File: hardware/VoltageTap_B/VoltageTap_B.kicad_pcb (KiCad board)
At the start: 2 copper layers, 154 parts, among them J1 Conn_01x09_Socket, J102 Conn_01x18_Pin, J15 Conn_02x04_Odd_Even, J16 USB_B_Micro, J2 Conn_02x05_Odd_Even, J3 Conn_01x04_Socket, Q6 2N7002, U10 MCP2542FDxMF, U12 FT230XS, U2 MCU-MSM0G3507SPM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

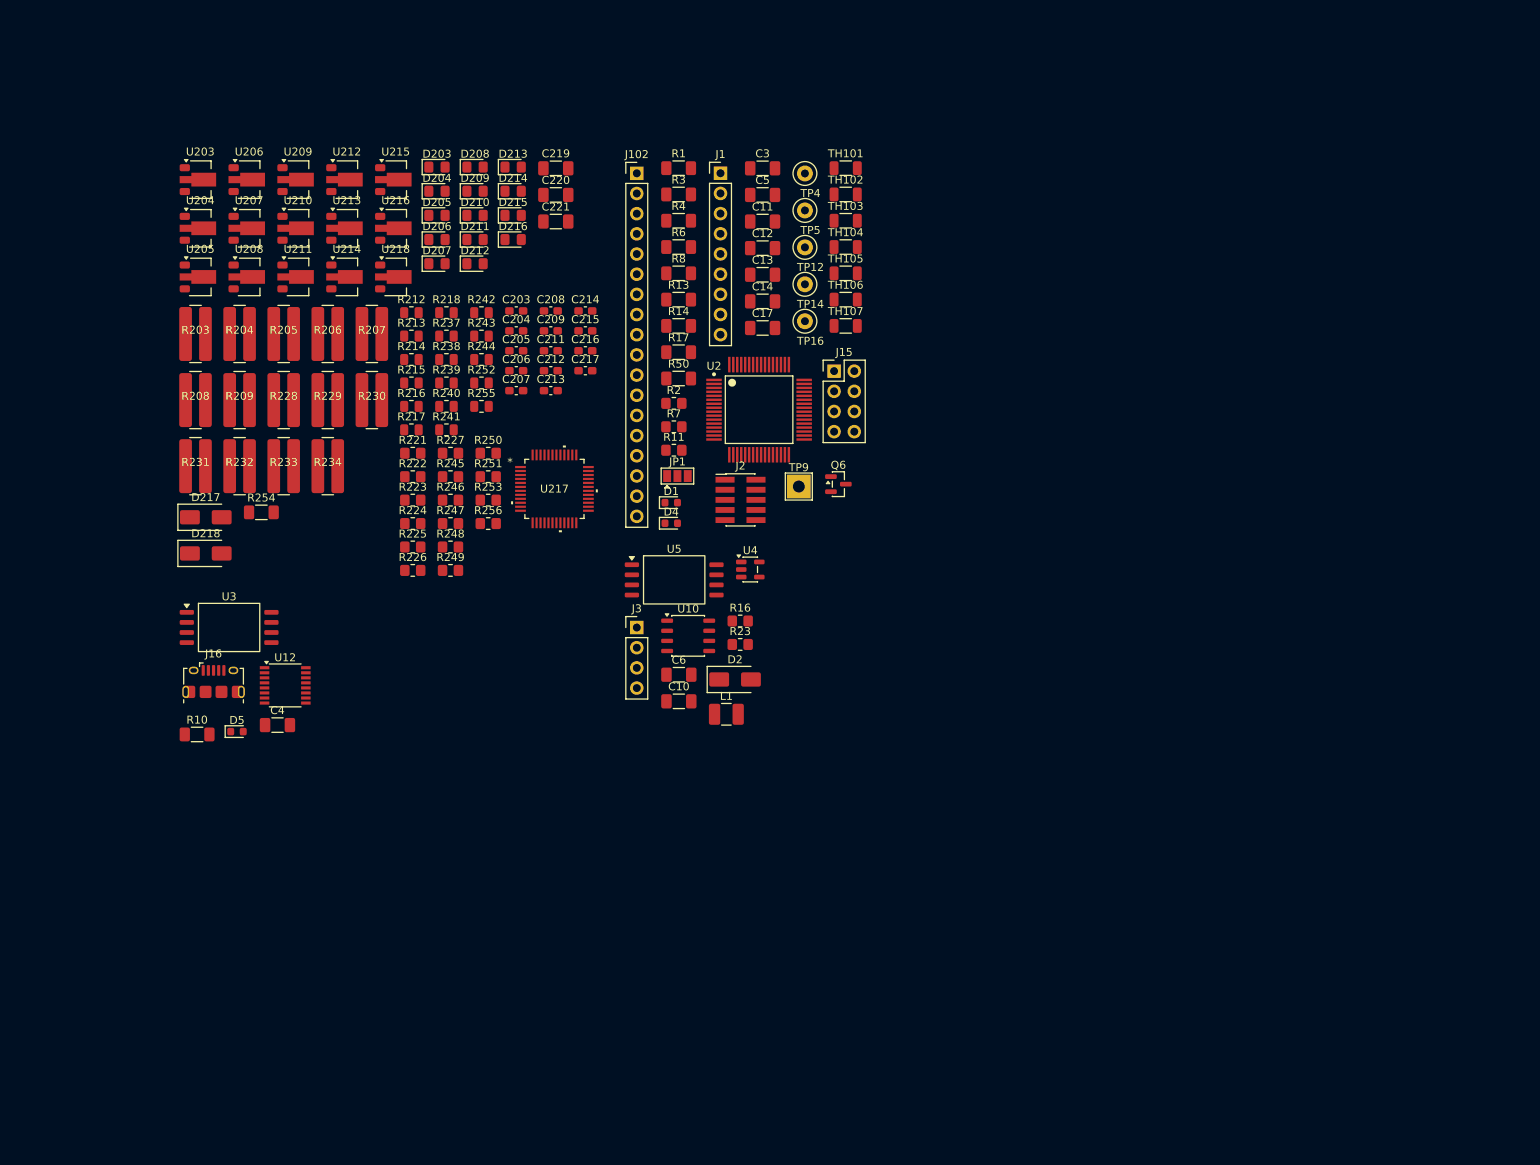
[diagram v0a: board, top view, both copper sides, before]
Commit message: voltage tap LV done. moving on.
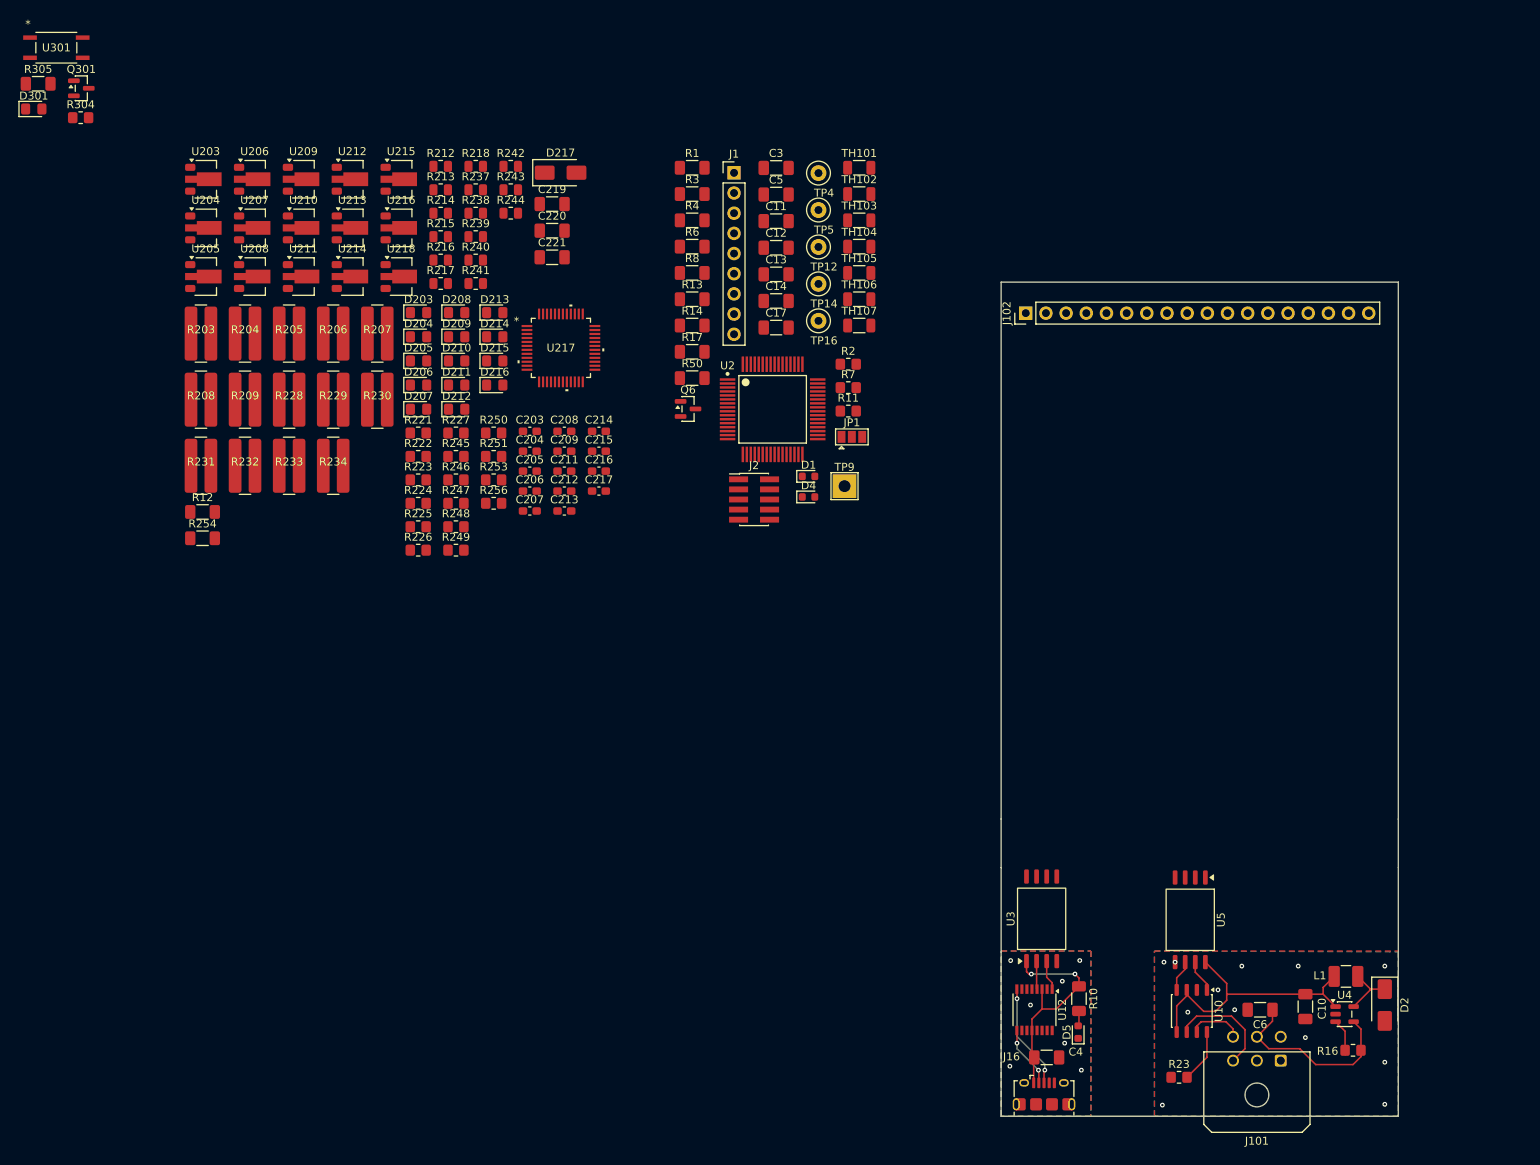
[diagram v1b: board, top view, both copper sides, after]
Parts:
- removed D218: ES1D, Diode_SMD:D_SMA
- removed J15: Conn_02x04_Odd_Even, Connector_PinHeader_2.54mm:PinHeader_2x04_P2.54mm_Vertical
- removed J3: Conn_01x04_Socket, Connector_PinHeader_2.54mm:PinHeader_1x04_P2.54mm_Vertical
- removed R252, R255: 100, Resistor_SMD:R_0805_2012Metric
- added D301: green, LED_SMD:LED_0805_2012Metric_Pad1.15x1.40mm_HandSolder, F.Cu at (1.92, 10.1)
- added J101: HRLV, Connector_Molex:Molex_Micro-Fit_3.0_43045-0600_2x03_P3.00mm_Horizontal, F.Cu at (158.9, 129.9)
- added Q301: MMBT5550L, Package_TO_SOT_SMD:SOT-23, F.Cu at (7.91, 7.50)
- added R12: 150, Resistor_SMD:R_1206_3216Metric_Pad1.30x1.75mm_HandSolder, F.Cu at (23.2, 60.8)
- added R304: 2.4k, Resistor_SMD:R_0805_2012Metric_Pad1.20x1.40mm_HandSolder, F.Cu at (7.83, 11.2)
- added R305: 750, Resistor_SMD:R_1206_3216Metric_Pad1.30x1.75mm_HandSolder, F.Cu at (2.48, 6.92)
- added U301: ISOM8600DFGR, zzLocalLibraries-Footprints:SOIC4_DFG_TEX-M, F.Cu at (4.76, 2.39)
- moved J16 116.7 mm to (129.1, 134.1)
- moved R10 115.9 mm to (133.5, 122.1), turned to -90 degrees
- moved D5 112.5 mm to (133.4, 126.3), turned to 90 degrees
- moved U3 108.7 mm to (128.8, 112.0), turned to 90 degrees
- moved C4 105.5 mm to (129.4, 129.5)
- moved U12 102.8 mm to (127.9, 123.5), turned to -90 degrees
- moved R16 94.2 mm to (168.0, 128.6)
- moved U4 93.4 mm to (166.9, 124.0)
- moved D2 91.5 mm to (172.0, 122.9), turned to -90 degrees
- moved C10 87.7 mm to (162.0, 123.1), turned to -90 degrees
- moved L1 84.7 mm to (167.1, 119.3), turned to 180 degrees
- moved C6 84.5 mm to (156.3, 123.5), turned to 180 degrees
- moved U10 79.1 mm to (147.7, 123.7), turned to -90 degrees
- moved U5 77.8 mm to (147.5, 112.2), turned to -90 degrees
- moved R23 77.6 mm to (146.1, 132.0)
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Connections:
- C221 pad 1: Net-(C221-Pad1) -> /BQ76952 1/BAT
- R13 pad 2: Net-(J15-Pin_1) -> PA18_SPI1_MOSI
- R14 pad 2: Net-(J15-Pin_3) -> PB19_BBQ_CS
- R17 pad 1: Net-(J15-Pin_7) -> PA16_SPI1_MISO
- R4 pad 1: Net-(J15-Pin_5) -> PA17_SPI1_SCK
- U10 pad 6: /GLV interface/CAN_L -> /GLV interface/CAN-
- U10 pad 7: /GLV interface/CAN_H -> /GLV interface/CAN+
- U218 pad 2: Net-(C221-Pad1) -> +BATT
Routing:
- net /GLV interface/5v: track 0.00 -> 36.0 mm
- net /UART_USB/5V: track 0.00 -> 27.6 mm, vias 0 -> 2
- net /GLV interface/GLV+: track 0.00 -> 24.6 mm
- net /GLV interface/CAN-: track 0.00 -> 13.8 mm
- net Net-(J16-D+): track 0.00 -> 13.3 mm, vias 0 -> 2
- net Net-(J16-D-): track 0.00 -> 7.85 mm, vias 0 -> 2
- net Net-(D2-K): track 0.00 -> 7.14 mm
- net /GLV interface/CAN+: track 0.00 -> 6.91 mm
- net Net-(U10-STBY): track 0.00 -> 6.74 mm
- net Net-(U4-EN): track 0.00 -> 4.70 mm
- net Net-(U10-TXD): track 0.00 -> 4.11 mm
- net Net-(U10-RXD): track 0.00 -> 3.94 mm
- net Net-(U12-TXD): track 0.00 -> 3.81 mm
- net Net-(U12-RXD): track 0.00 -> 3.55 mm
- net Net-(D5-A): track 0.00 -> 1.92 mm
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- added copper zone on B.Cu, net /GLV interface/GLV-
- added copper zone on F.Cu, net /GLV interface/GLV-
- added copper zone on B.Cu, net /UART_USB/GND
- added copper zone on F.Cu, net /UART_USB/GND
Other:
- board outline added: 50 x 105 mm

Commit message: Almost done with Voltage Tap Bee...
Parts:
- removed D301: green, LED_SMD:LED_0805_2012Metric_Pad1.15x1.40mm_HandSolder
- removed J2: Conn_02x05_Odd_Even, Connector_PinHeader_1.27mm:PinHeader_2x05_P1.27mm_Vertical_SMD
- removed Q301: MMBT5550L, Package_TO_SOT_SMD:SOT-23
- removed R304: 2.4k, Resistor_SMD:R_0805_2012Metric_Pad1.20x1.40mm_HandSolder
- removed R305: 750, Resistor_SMD:R_1206_3216Metric_Pad1.30x1.75mm_HandSolder
- removed TP12, TP14, TP16, TP4, TP5: TestPoint, TestPoint:TestPoint_Loop_D2.50mm_Drill1.0mm_LowProfile
- removed TP9: TestPoint, TestPoint:TestPoint_THTPad_3.0x3.0mm_Drill1.5mm
- removed U301: ISOM8600DFGR, zzLocalLibraries-Footprints:SOIC4_DFG_TEX-M
- moved U207 150.3 mm to (169.6, 80.3), turned to 90 degrees
- moved U206 149.3 mm to (169.6, 71.3), turned to 90 degrees
- moved U205 149.3 mm to (169.6, 62.3), turned to 90 degrees
- moved U204 148.7 mm to (169.6, 53.3), turned to 90 degrees
- moved U203 148.2 mm to (169.6, 44.3), turned to 90 degrees
- moved U218 140.1 mm to (171.1, 98.3)
- moved R203 139.7 mm to (162.7, 42.0), turned to -90 degrees
- moved R212 139.4 mm to (171.6, 90.8)
- moved R204 134.7 mm to (162.7, 51.0), turned to -90 degrees
- moved R205 130.4 mm to (162.7, 60.0), turned to -90 degrees
- moved U212 127.1 mm to (153.4, 80.3), turned to 90 degrees
- moved R206 126.8 mm to (162.7, 69.0), turned to -90 degrees
- moved R217 125.4 mm to (170.3, 76.7), turned to 180 degrees
- moved U208 124.3 mm to (153.4, 44.0), turned to 90 degrees
- moved U211 124.1 mm to (153.4, 71.0), turned to 90 degrees
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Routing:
- net /BQ76952 1/4P: track 0.00 -> 87.1 mm
- net /BQ76952 1/9P: track 0.00 -> 86.0 mm
- net +BATT: track 0.00 -> 84.5 mm
- net Net-(U217-VC3): track 0.00 -> 79.8 mm, vias 0 -> 2
- net Net-(U217-VC2): track 0.00 -> 75.7 mm, vias 0 -> 2
- net -BATT: track 0.00 -> 71.2 mm
- net Net-(U217-VC1): track 0.00 -> 70.8 mm, vias 0 -> 2
- net /BQ76952 1/10P: track 0.00 -> 69.5 mm
- net /BQ76952 1/5P: track 0.00 -> 66.9 mm
- net Net-(U217-VC8): track 0.00 -> 66.7 mm, vias 0 -> 2
- net Net-(U217-VC13): track 0.00 -> 65.9 mm, vias 0 -> 3
- net Net-(U217-VC7): track 0.00 -> 60.3 mm, vias 0 -> 2
- net /BQ76952 1/1P: track 0.00 -> 59.1 mm
- net /BQ76952 1/11P: track 0.00 -> 58.6 mm
- net /BQ76952 1/6P: track 0.00 -> 56.9 mm
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- added copper zone on B.Cu, net -BATT
- added copper zone on F.Cu, net -BATT
- added copper zone on B.Cu, net /BQ76952 1/C10Jc
- added copper zone on F.Cu, net /BQ76952 1/C10Jc
- added copper zone on B.Cu, net /BQ76952 1/C11Jc
- added copper zone on F.Cu, net /BQ76952 1/C11Jc
- added copper zone on B.Cu, net /BQ76952 1/C12Jc
- added copper zone on F.Cu, net /BQ76952 1/C12Jc
- added copper zone on B.Cu, net /BQ76952 1/C13Jc
- added copper zone on F.Cu, net /BQ76952 1/C13Jc
- added copper zone on B.Cu, net /BQ76952 1/C14Jc
- added copper zone on F.Cu, net /BQ76952 1/C14Jc
- added copper zone on B.Cu, net /BQ76952 1/C1Jc
- added copper zone on F.Cu, net /BQ76952 1/C1Jc
- added copper zone on B.Cu, net /BQ76952 1/C2Jc
- added copper zone on F.Cu, net /BQ76952 1/C2Jc
- added copper zone on B.Cu, net /BQ76952 1/C3Jc
- added copper zone on F.Cu, net /BQ76952 1/C3Jc
- added copper zone on B.Cu, net /BQ76952 1/C4Jc
- added copper zone on F.Cu, net /BQ76952 1/C4Jc
- added copper zone on B.Cu, net /BQ76952 1/C5Jc
- added copper zone on F.Cu, net /BQ76952 1/C5Jc
- added copper zone on B.Cu, net /BQ76952 1/C6Jc
- added copper zone on F.Cu, net /BQ76952 1/C6Jc
- added copper zone on B.Cu, net /BQ76952 1/C7Jc
- added copper zone on F.Cu, net /BQ76952 1/C7Jc
- added copper zone on B.Cu, net /BQ76952 1/C8Jc
- added copper zone on F.Cu, net /BQ76952 1/C8Jc
- added copper zone on B.Cu, net /BQ76952 1/C9Jc
- added copper zone on F.Cu, net /BQ76952 1/C9Jc
